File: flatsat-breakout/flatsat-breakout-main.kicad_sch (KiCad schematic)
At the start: 5 parts, among them J1 SFM-120-02-L-DH-TR, J2 61204021621, J3 61204021621, J4 68000-227HLF, J5 Conn_02x08_Odd_Even

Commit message: Updates to schematic
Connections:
- net C3-UART-RX: now also J1.38 (Pin_38), J2.38 (Pin_38), J3.38 (Pin_38), J4.26 (Pin_26)
- net C3-UART-TX: now also J1.37 (Pin_37), J2.37 (Pin_37), J3.37 (Pin_37), J4.25 (Pin_25)
- net CAN1_H: now also J1.33 (Pin_33), J1.34 (Pin_34), J2.33 (Pin_33), J2.34 (Pin_34), J3.33 (Pin_33), J3.34 (Pin_34), J4.23 (Pin_23)
- net CAN1_L: now also J1.35 (Pin_35), J1.36 (Pin_36), J2.35 (Pin_35), J2.36 (Pin_36), J3.35 (Pin_35), J3.36 (Pin_36), J4.24 (Pin_24)
- net CAN2_H: now also J1.17 (Pin_17), J1.18 (Pin_18), J2.17 (Pin_17), J2.18 (Pin_18), J3.17 (Pin_17), J3.18 (Pin_18), J4.13 (Pin_13)
- net CAN2_L: now also J1.19 (Pin_19), J1.20 (Pin_20), J2.19 (Pin_19), J2.20 (Pin_20), J3.19 (Pin_19), J3.20 (Pin_20), J4.14 (Pin_14)
- net OPD_PWR: now also J1.15 (Pin_15), J1.16 (Pin_16), J2.15 (Pin_15), J2.16 (Pin_16), J3.15 (Pin_15), J3.16 (Pin_16), J4.12 (Pin_12)
- net OPD_SCL: now also J1.13 (Pin_13), J1.14 (Pin_14), J2.13 (Pin_13), J2.14 (Pin_14), J3.13 (Pin_13), J3.14 (Pin_14), J4.11 (Pin_11)
- net OPD_SDA: now also J1.11 (Pin_11), J1.12 (Pin_12), J2.11 (Pin_11), J2.12 (Pin_12), J3.11 (Pin_11), J3.12 (Pin_12), J4.10 (Pin_10)
- net VBUS: now also J2.23 (Pin_23), J2.24 (Pin_24), J2.25 (Pin_25), J2.26 (Pin_26), J3.23 (Pin_23), J3.24 (Pin_24), J3.25 (Pin_25), J3.26 (Pin_26), J4.17 (Pin_17), J4.18 (Pin_18)
- net MAG-SDA: now reaches J1.1 (Pin_1), J1.2 (Pin_2), J2.1 (Pin_1), J2.2 (Pin_2), J3.1 (Pin_1), J3.2 (Pin_2), J4.1 (Pin_1)
- net TURNSTILE-DEPLOY: now reaches J2.10 (Pin_10), J3.10 (Pin_10), J4.9 (Pin_9)
- net TURNSTILE-DEPLOY: now also J1.10 (Pin_10), J1.9 (Pin_9), J2.9 (Pin_9), J3.9 (Pin_9)
- net SPARE21: now reaches J1.21 (Pin_21), J2.21 (Pin_21), J3.21 (Pin_21)
- net SPARE21: no longer J4.15 (Pin_15)
- net SPARE22: now reaches J1.22 (Pin_22), J2.22 (Pin_22), J3.22 (Pin_22)
- net SPARE22: no longer J4.16 (Pin_16)
- net MAG-SCL: now reaches J1.3 (Pin_3), J1.4 (Pin_4), J2.3 (Pin_3), J3.3 (Pin_3)
- net MAG-SCL: now also J2.4 (Pin_4), J3.4 (Pin_4), J4.3 (Pin_3); no longer J4.2 (Pin_2)
- net SPARE31: now reaches J1.31 (Pin_31), J2.31 (Pin_31), J3.31 (Pin_31)
- net SPARE31: no longer J4.21 (Pin_21)
- net SPARE32: now reaches J1.32 (Pin_32), J2.32 (Pin_32), J3.32 (Pin_32)
- net SPARE32: no longer J4.22 (Pin_22)
- net MAG-POWER: now reaches J1.5 (Pin_5), J1.6 (Pin_6), J2.5 (Pin_5), J3.5 (Pin_5)
- net MAG-POWER: now also J2.6 (Pin_6), J3.6 (Pin_6), J4.5 (Pin_5); no longer J4.4 (Pin_4)
- net HELICAL-DEPLOY: now reaches J1.7 (Pin_7), J1.8 (Pin_8), J2.7 (Pin_7), J3.7 (Pin_7)
- net HELICAL-DEPLOY: now also J2.8 (Pin_8), J3.8 (Pin_8), J4.7 (Pin_7); no longer J4.6 (Pin_6)
- now unconnected: J4.8 (Pin_8)
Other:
- note removed: "C3-UART-RX"
- note removed: "C3-UART-TX"
- note removed: "CAN1_L"
- note removed: "HELICAL-DEPLOY"
- note removed: "MAG-POWER"
- note removed: "MAG-SCL"
- note removed: "MAG-SDA"
- note removed: "OPD_SDA"
- note removed: "SPARE21"
- note removed: "SPARE22"
- note removed: "SPARE31"
- note removed: "SPARE32"
- note removed: "TURNSTILE-DEPLOY"
- moved on the sheet: J4

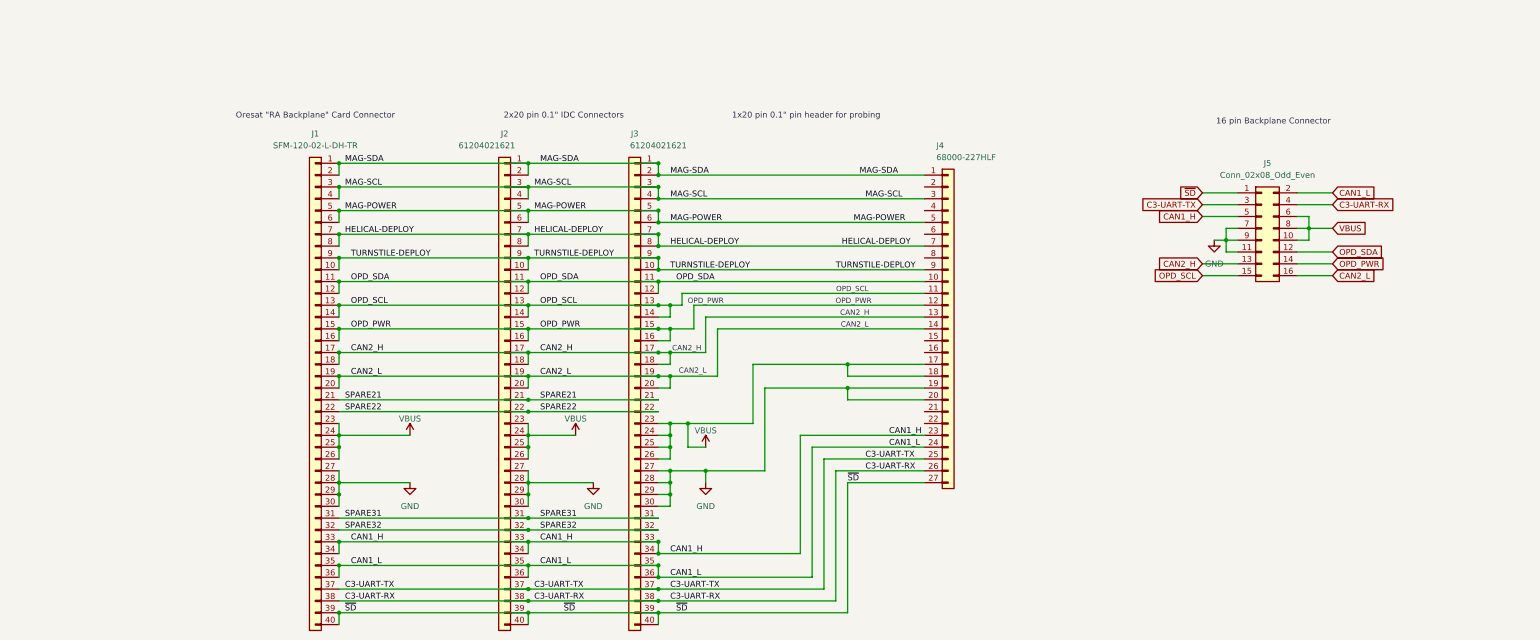
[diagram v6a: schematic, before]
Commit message: Update flatsat-breakout schematic wiring
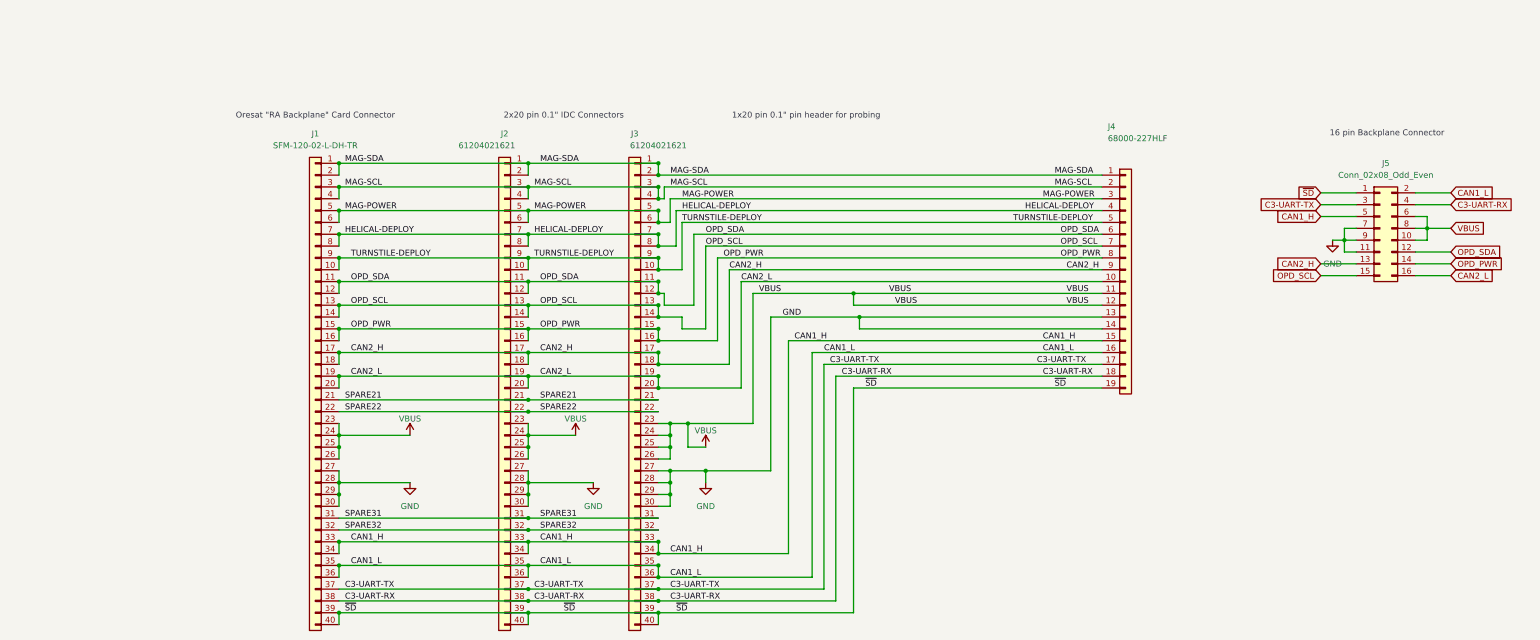
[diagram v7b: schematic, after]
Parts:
- removed J4: 68000-227HLF, Connector_PinHeader_2.54mm:PinHeader_1x27_P2.54mm_Vertical, symbol Connector_Generic:Conn_01x27
- added J4: 68000-227HLF, Connector_PinHeader_2.54mm:PinHeader_1x27_P2.54mm_Vertical, symbol Connector_Generic:Conn_01x19
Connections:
- net C3-UART-RX: now also J4.18 (Pin_18)
- net C3-UART-TX: now also J4.17 (Pin_17)
- net CAN1_H: now also J4.15 (Pin_15)
- net CAN1_L: now also J4.16 (Pin_16)
- net CAN2_H: now also J4.9 (Pin_9)
- net CAN2_L: now also J4.10 (Pin_10)
- net GND: now also J4.13 (Pin_13), J4.14 (Pin_14)
- net HELICAL-DEPLOY: now also J4.4 (Pin_4)
- net MAG-POWER: now also J4.3 (Pin_3)
- net MAG-SCL: now also J4.2 (Pin_2)
- net MAG-SDA: now also J4.1 (Pin_1)
- net OPD_PWR: now also J4.8 (Pin_8)
- net OPD_SCL: now also J4.7 (Pin_7)
- net OPD_SDA: now also J4.6 (Pin_6)
- net TURNSTILE-DEPLOY: now also J4.5 (Pin_5)
- net VBUS: now also J4.11 (Pin_11), J4.12 (Pin_12)
- net ~{SD}: now also J4.19 (Pin_19)
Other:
- note removed: "CAN2_H"
- note removed: "CAN2_L"
- note removed: "OPD_PWR"
- note removed: "OPD_SCL"
- moved on the sheet: J5

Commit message: Helped polish schematic, passes ERC, ready for layout.
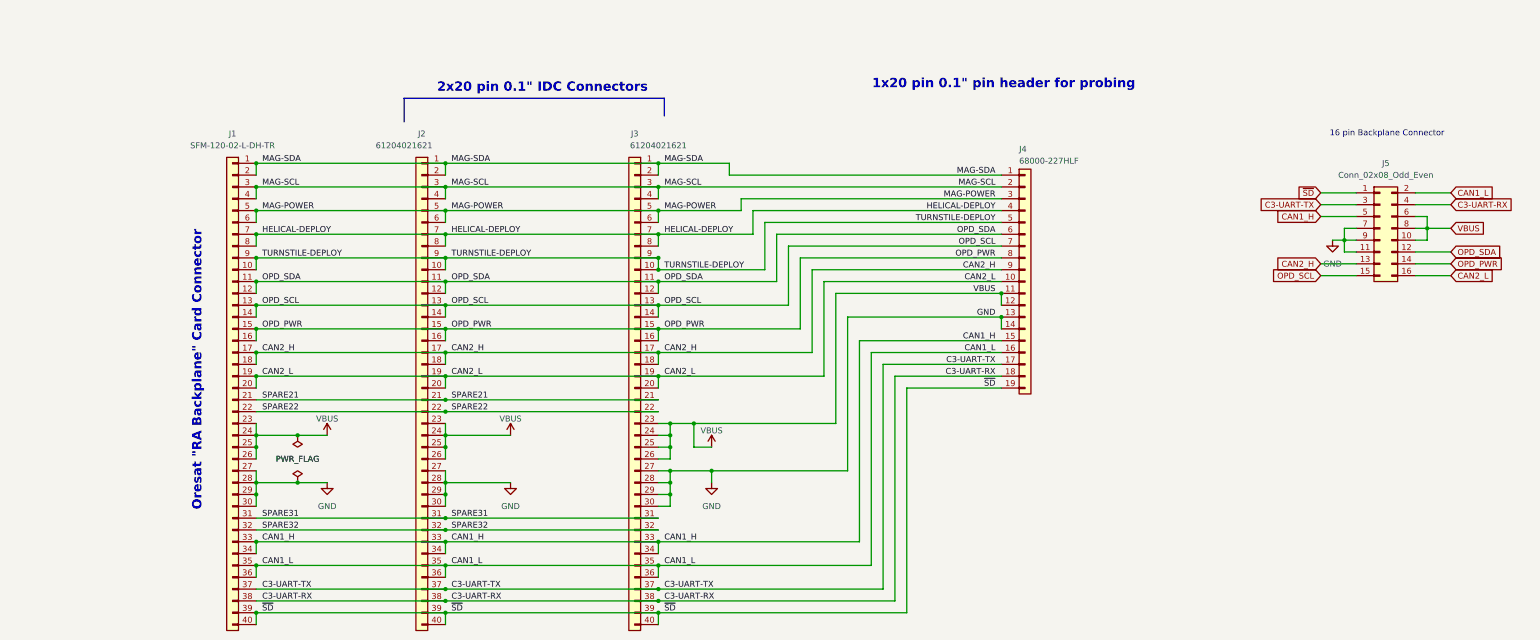
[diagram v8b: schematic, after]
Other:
- moved on the sheet: J1, J2, J4
